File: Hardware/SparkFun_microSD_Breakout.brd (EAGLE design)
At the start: 21.6 x 22.9 mm, 7 parts, among them U1 microSD

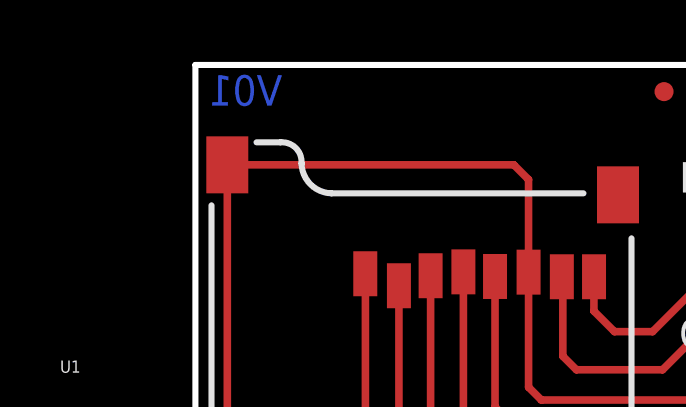
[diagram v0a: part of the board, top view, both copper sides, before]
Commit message: Fixed pin out.
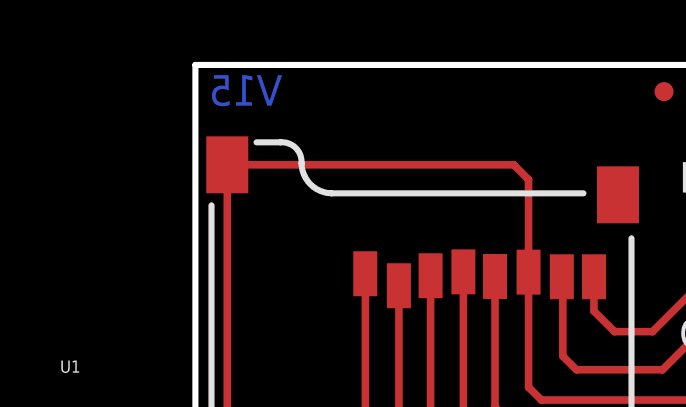
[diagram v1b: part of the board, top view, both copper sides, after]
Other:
- board text added: "V15"
- board text removed: "V01"
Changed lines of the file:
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@@
 <setting verticaltext="up"/>
 </settings>
-<grid distance="0.05" unitdist="inch" unit="inch" style="lines" multiple="1" display="yes" altdistance="0.0001" altunitdist="inch" altunit="inch"/>
+<grid distance="0.05" unitdist="inch" unit="inch" style="lines" multiple="1" display="yes" altdistance="0.005" altunitdist="inch" altunit="inch"/>
 <layers>
 <layer number="1" name="Top" color="4" fill="1" visible="yes" active="yes"/>
@@
 <layer number="45" name="Holes" color="7" fill="1" visible="yes" active="yes"/>
 <layer number="46" name="Milling" color="3" fill="1" visible="no" active="yes"/>
-<layer number="47" name="Measures" color="7" fill="1" visible="yes" active="yes"/>
+<layer number="47" name="Measures" color="7" fill="1" visible="no" active="yes"/>
 <layer number="48" name="Document" color="7" fill="1" visible="no" active="yes"/>
-<layer number="49" name="Reference" color="7" fill="1" visible="yes" active="yes"/>
+<layer number="49" name="Reference" color="7" fill="1" visible="no" active="yes"/>
 <layer number="50" name="dxf" color="7" fill="1" visible="no" active="yes"/>
 <layer number="51" name="tDocu" color="6" fill="1" visible="yes" active="yes"/>
@@
 <text x="18.679159375" y="18.608040625" size="1.016" layer="22" font="vector" ratio="15" rot="MR0">RSV</text>
 <text x="18.61311875" y="0.762003125" size="1.016" layer="22" font="vector" ratio="15" rot="MR0">NC</text>
-<text x="2.8956" y="21.503640625" size="1.016" layer="16" font="vector" rot="MR0">V01</text>
+<text x="2.8956" y="21.503640625" size="1.016" layer="16" font="vector" rot="MR0">V15</text>
 </plain>
 <attributes>
